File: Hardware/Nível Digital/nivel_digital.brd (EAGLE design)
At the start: 68.6 x 53.3 mm, 11 parts, among them IC1 MODULO_ADXL345

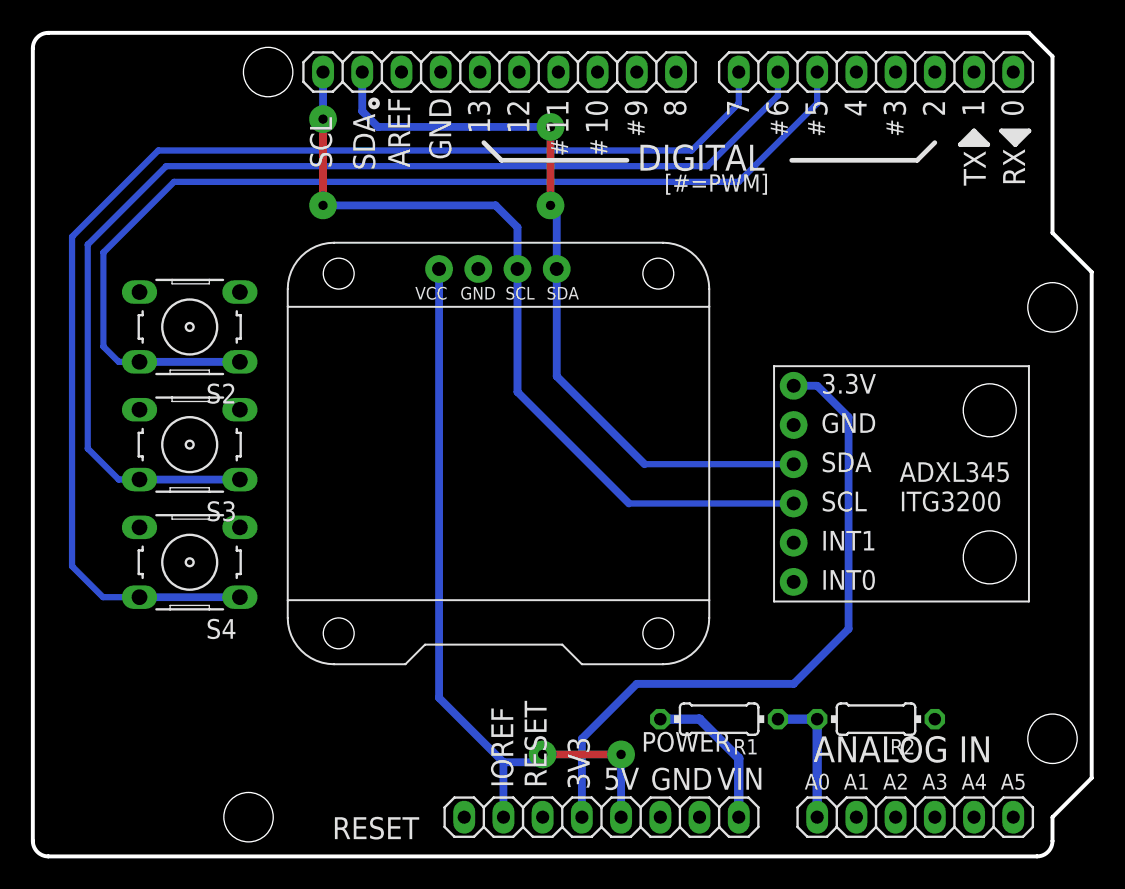
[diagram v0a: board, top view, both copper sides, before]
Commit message: Display e acelerômetro novos
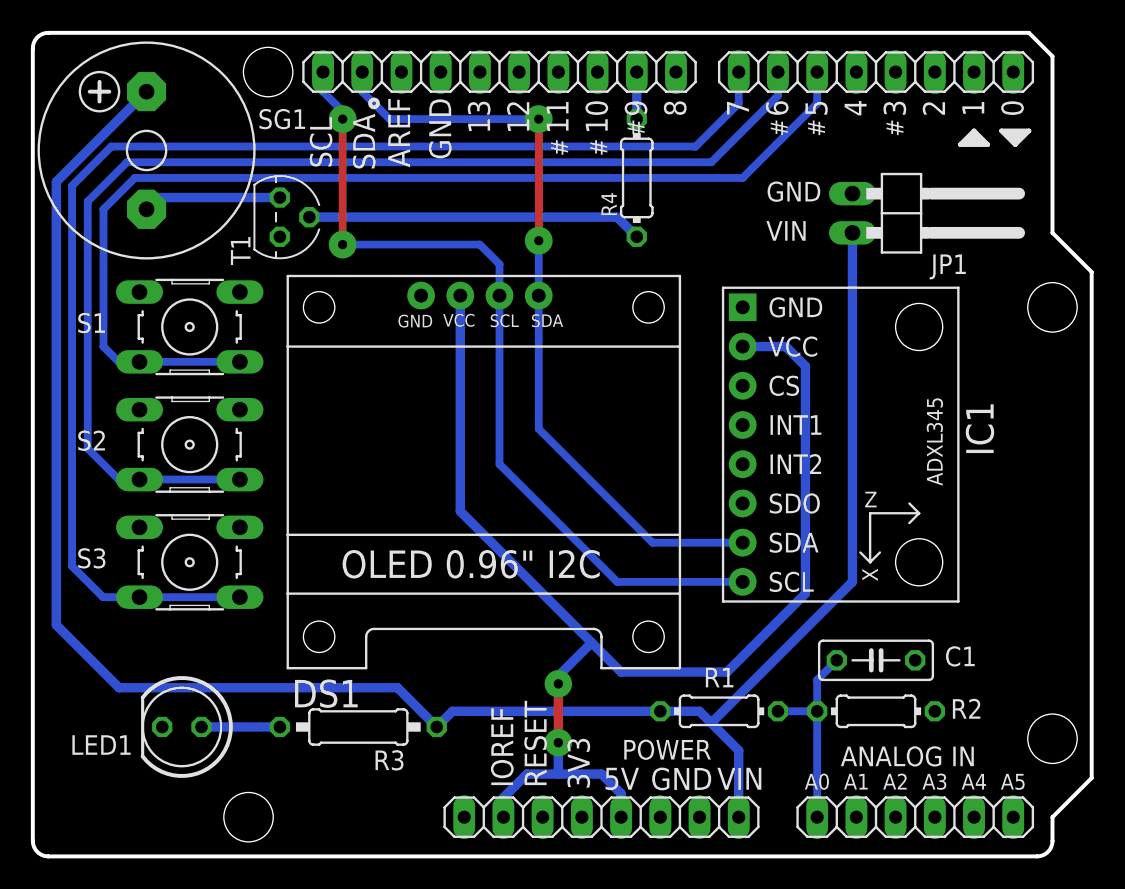
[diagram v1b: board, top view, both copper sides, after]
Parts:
- removed S4: (no value), GEAP:B3F-10XX
- added C1: (no value), rcl:C050-025X075
- added JP1: (no value), pinhead:1X02/90
- added LED1: (no value), led:LED5MM
- added R3: (no value), rcl:0207/10
- added R4: (no value), rcl:0204/7
- added S1: (no value), GEAP:B3F-10XX
- added SG1: F/CM12P, buzzer:F/CM12P
- added T1: BC337, transistor:TO92
- moved S3 7.62 mm to (10.2, 19.1)
- moved S2 7.62 mm to (10.2, 26.7)
- moved IC1 3.30 mm to (44.7, 16.5)
- moved DS1 1.98 mm to (29.2, 24.9)
- moved R1 0.51 mm to (44.5, 9.40)
- moved R2 0.51 mm to (54.6, 9.40)
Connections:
- new net N$1: LED1.A, R3.2
- new net N$2: SG1.-, T1.3
- new net N$3: R4.1, T1.2
- net +3V3: no longer IC1.1
- net +5V: now also DS1.2, IC1.2; no longer DS1.1
- net AD0: now also C1.1
- net AD4/SDA: now also IC1.7; no longer IC1.3
- net AD5/SCL: now also IC1.8; no longer IC1.4
- net GND: now also C1.2, DS1.1, IC1.1, JP1.1, LED1.K, S1.3, S1.4, T1.1; no longer DS1.2, IC1.2, S4.3, S4.4
- net IO5: now also S1.1, S1.2; no longer S2.1, S2.2
- net IO6: now also S2.1, S2.2; no longer S3.1, S3.2
- net IO7: now also S3.1, S3.2; no longer S4.1, S4.2
- net IO9: now also R4.2
- net VIN: now also JP1.2, R3.1, SG1.+
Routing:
- net VIN: track 9.94 -> 125.2 mm
- net +3V3: track 43.4 -> 0.00 mm
- net +5V: track 49.1 -> 83.0 mm
- net N$3: track 0.00 -> 21.7 mm
- net N$2: track 0.00 -> 8.95 mm
- net N$1: track 0.00 -> 5.08 mm
- net AD0: track 8.89 -> 13.2 mm
- net IO9: track 0.00 -> 3.05 mm
- net IO7: track 81.8 -> 83.8 mm
- net IO5: track 67.6 -> 69.2 mm
- net IO6: track 74.1 -> 75.8 mm
- net AD5/SCL: track 53.4 -> 54.2 mm
- net AD4/SDA: track 49.2 -> 49.8 mm
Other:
- board text removed: "DIGITAL"
- board text removed: "RX"
- board text removed: "TX"
- board text removed: "[#=PWM]"
